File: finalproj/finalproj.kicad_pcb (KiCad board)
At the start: 2 copper layers, 99.2 x 99.6 mm, 83 parts, among them J1 Conn_01x01, J10 MotorA Out, J11 MotorB Out, J2 Conn_01x01, J3 Conn_01x01, J4 Programmer_Conn, J5 Stepper_Motor_Controller, J6 Conn_01x01, J7 LIDAR_Connector, J9 RPI_UART_Conn, SW1 SW_DPDT_x2, SW2 SW_DPDT_x2, SW3 SW_Push, U1 LM1085-12, U2 LM1085-12, U3 LM1085-5.0, U4 LM1085-3.3, U5 L298N, U7 STM32F401RCTx, Y1 25 MHz, Y2 32.768 KHz

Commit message: fixed switch footprints
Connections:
- RV1 pad 1: EXT_GND -> Net-(U3-GND)
- RV1 pad 2: unconnected-(RV1-Pad2) -> EXT_GND
- RV1 pad 3: Net-(U3-GND) -> unconnected-(RV1-Pad3)
- RV3 pad 1: EXT_GND -> Net-(U4-GND)
- RV3 pad 2: unconnected-(RV3-Pad2) -> EXT_GND
- RV3 pad 3: Net-(U4-GND) -> unconnected-(RV3-Pad3)
- RV4 pad 1: EXT_GND -> Net-(U1-GND)
- RV4 pad 2: unconnected-(RV4-Pad2) -> EXT_GND
- RV4 pad 3: Net-(U1-GND) -> unconnected-(RV4-Pad3)
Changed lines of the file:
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@@
   (net 30 "Net-(U7-PH1)")
   (net 31 "Net-(U7-PH0)")
-  (net 32 "unconnected-(RV1-Pad2)")
+  (net 32 "unconnected-(RV1-Pad3)")
   (net 33 "unconnected-(RV2-Pad2)")
-  (net 34 "unconnected-(RV3-Pad2)")
+  (net 34 "unconnected-(RV3-Pad3)")
   (net 35 "unconnected-(U7-PC13-Pad2)")
   (net 36 "unconnected-(U7-PC0-Pad8)")
@@
   (net 80 "Net-(U4-GND)")
   (net 81 "Net-(U1-GND)")
-  (net 82 "unconnected-(RV4-Pad2)")
+  (net 82 "unconnected-(RV4-Pad3)")
   (footprint "Connector_PinHeader_2.54mm:PinHeader_1x01_P2.54mm_Vertical" (layer "F.Cu")
     (at 15.4 46.8 -90)
@@
       (stroke (width 0.1) (type solid)) (fill none) (layer "F.Fab"))
     (pad "1" smd rect (at -1.8 -1) (size 1.2 1.2) (layers "F.Cu" "F.Paste" "F.Mask")
-      (net 3 "EXT_GND") (pinfunction "1") (pintype "passive"))
+      (net 79 "Net-(U3-GND)") (pinfunction "1") (pintype "passive"))
     (pad "2" smd rect (at 1.45 0) (size 1.5 1.6) (layers "F.Cu" "F.Paste" "F.Mask")
-      (net 32 "unconnected-(RV1-Pad2)") (pinfunction "2") (pintype "passive"))
+      (net 3 "EXT_GND") (pinfunction "2") (pintype "passive"))
     (pad "3" smd rect (at -1.8 1) (size 1.2 1.2) (layers "F.Cu" "F.Paste" "F.Mask")
-      (net 79 "Net-(U3-GND)") (pinfunction "3") (pintype "passive"))
+      (net 32 "unconnected-(RV1-Pad3)") (pinfunction "3") (pintype "passive"))
     (model "${KICAD6_3DMODEL_DIR}/Potentiometer_SMD.3dshapes/Potentiometer_Bourns_TC33X_Vertical.wrl"
       (offset (xyz 0 0 0))
@@
       (stroke (width 0.1) (type solid)) (fill none) (layer "F.Fab"))
     (pad "1" smd rect (at -1.8 -1) (size 1.2 1.2) (layers "F.Cu" "F.Paste" "F.Mask")
-      (net 3 "EXT_GND") (pinfunction "1") (pintype "passive"))
+      (net 80 "Net-(U4-GND)") (pinfunction "1") (pintype "passive"))
     (pad "2" smd rect (at 1.45 0) (size 1.5 1.6) (layers "F.Cu" "F.Paste" "F.Mask")
-      (net 34 "unconnected-(RV3-Pad2)") (pinfunction "2") (pintype "passive"))
+      (net 3 "EXT_GND") (pinfunction "2") (pintype "passive"))
     (pad "3" smd rect (at -1.8 1) (size 1.2 1.2) (layers "F.Cu" "F.Paste" "F.Mask")
-      (net 80 "Net-(U4-GND)") (pinfunction "3") (pintype "passive"))
+      (net 34 "unconnected-(RV3-Pad3)") (pinfunction "3") (pintype "passive"))
     (model "${KICAD6_3DMODEL_DIR}/Potentiometer_SMD.3dshapes/Potentiometer_Bourns_TC33X_Vertical.wrl"
       (offset (xyz 0 0 0))
@@
       (stroke (width 0.1) (type solid)) (fill none) (layer "F.Fab"))
     (pad "1" smd rect (at -1.8 -1 90) (size 1.2 1.2) (layers "F.Cu" "F.Paste" "F.Mask")
-      (net 3 "EXT_GND") (pinfunction "1") (pintype "passive"))
+      (net 81 "Net-(U1-GND)") (pinfunction "1") (pintype "passive"))
     (pad "2" smd rect (at 1.45 0 90) (size 1.5 1.6) (layers "F.Cu" "F.Paste" "F.Mask")
-      (net 82 "unconnected-(RV4-Pad2)") (pinfunction "2") (pintype "passive"))
+      (net 3 "EXT_GND") (pinfunction "2") (pintype "passive"))
     (pad "3" smd rect (at -1.8 1 90) (size 1.2 1.2) (layers "F.Cu" "F.Paste" "F.Mask")
-      (net 81 "Net-(U1-GND)") (pinfunction "3") (pintype "passive"))
+      (net 82 "unconnected-(RV4-Pad3)") (pinfunction "3") (pintype "passive"))
     (model "${KICAD6_3DMODEL_DIR}/Potentiometer_SMD.3dshapes/Potentiometer_Bourns_TC33X_Vertical.wrl"
       (offset (xyz 0 0 0))

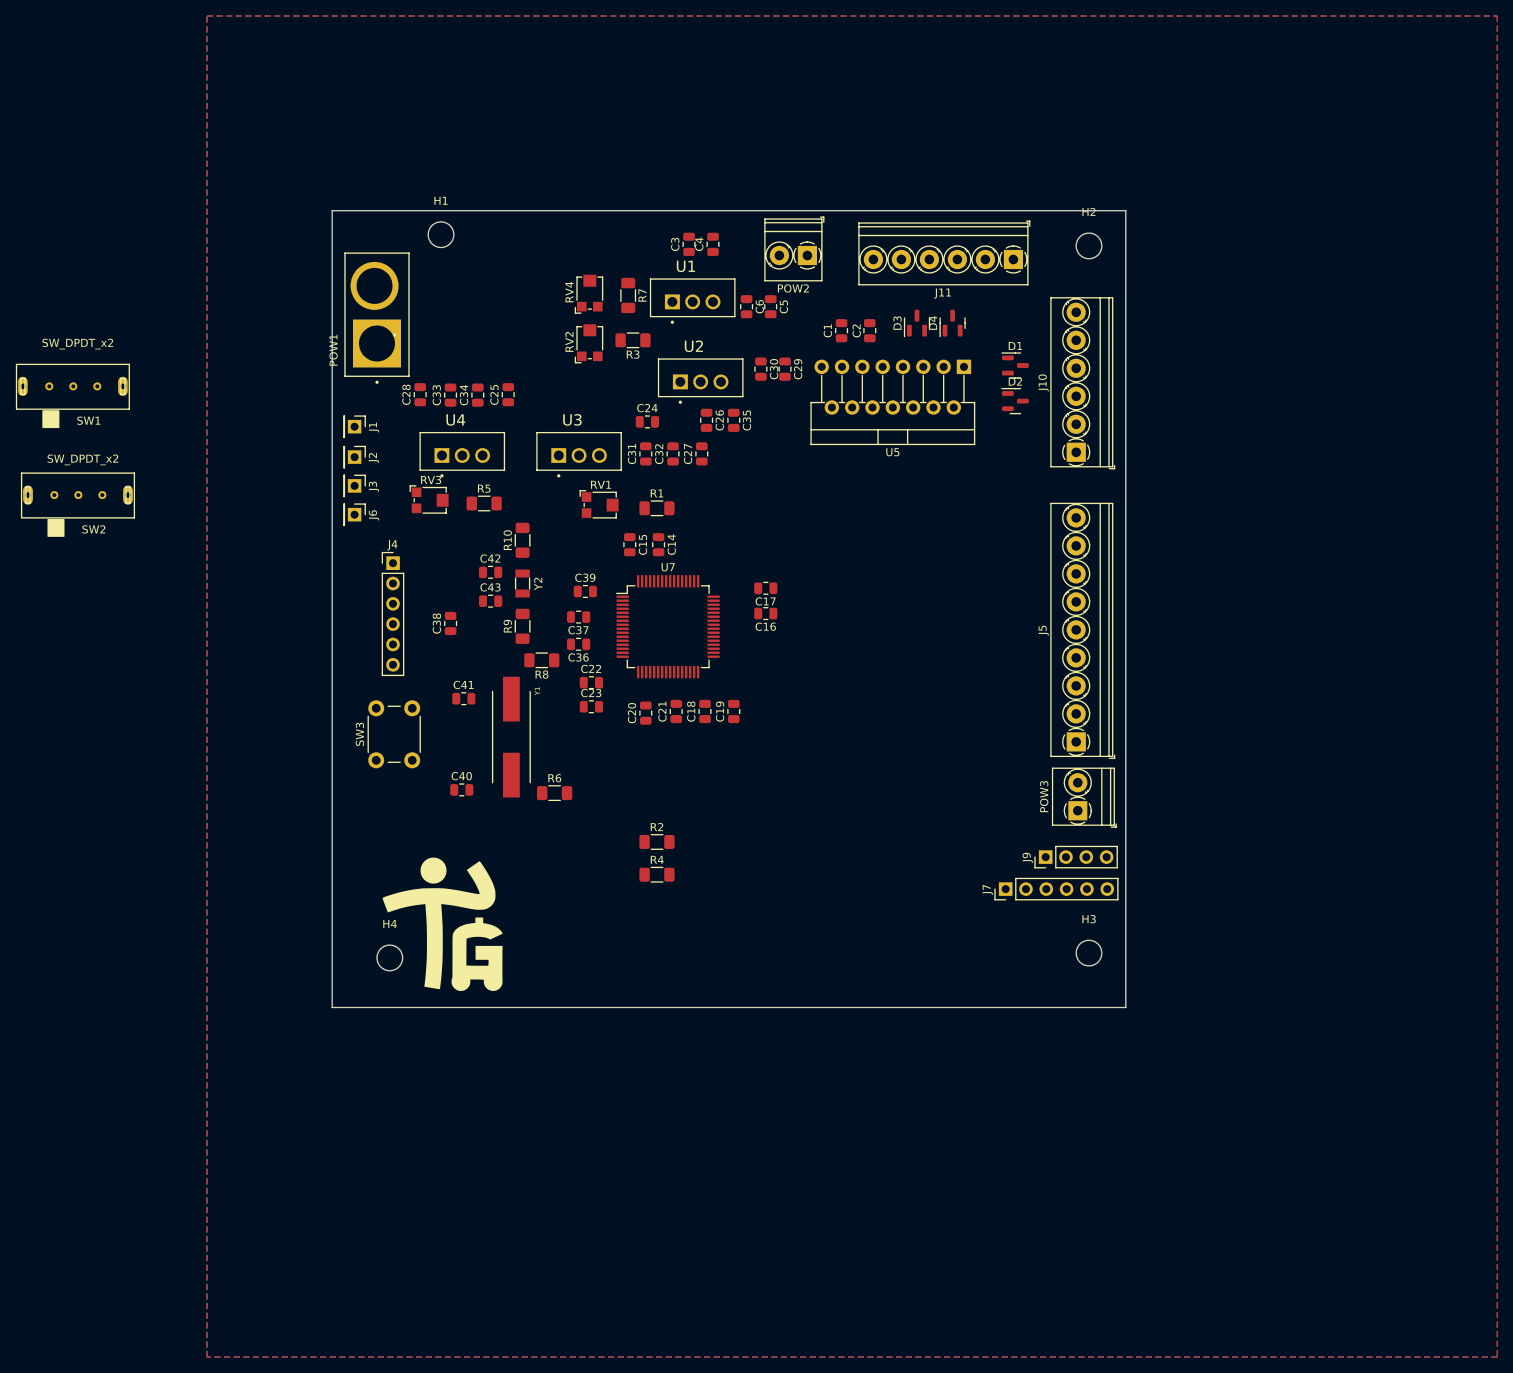
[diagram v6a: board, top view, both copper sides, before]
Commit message: made initial placement for each component on PCB, connected MCU passive components
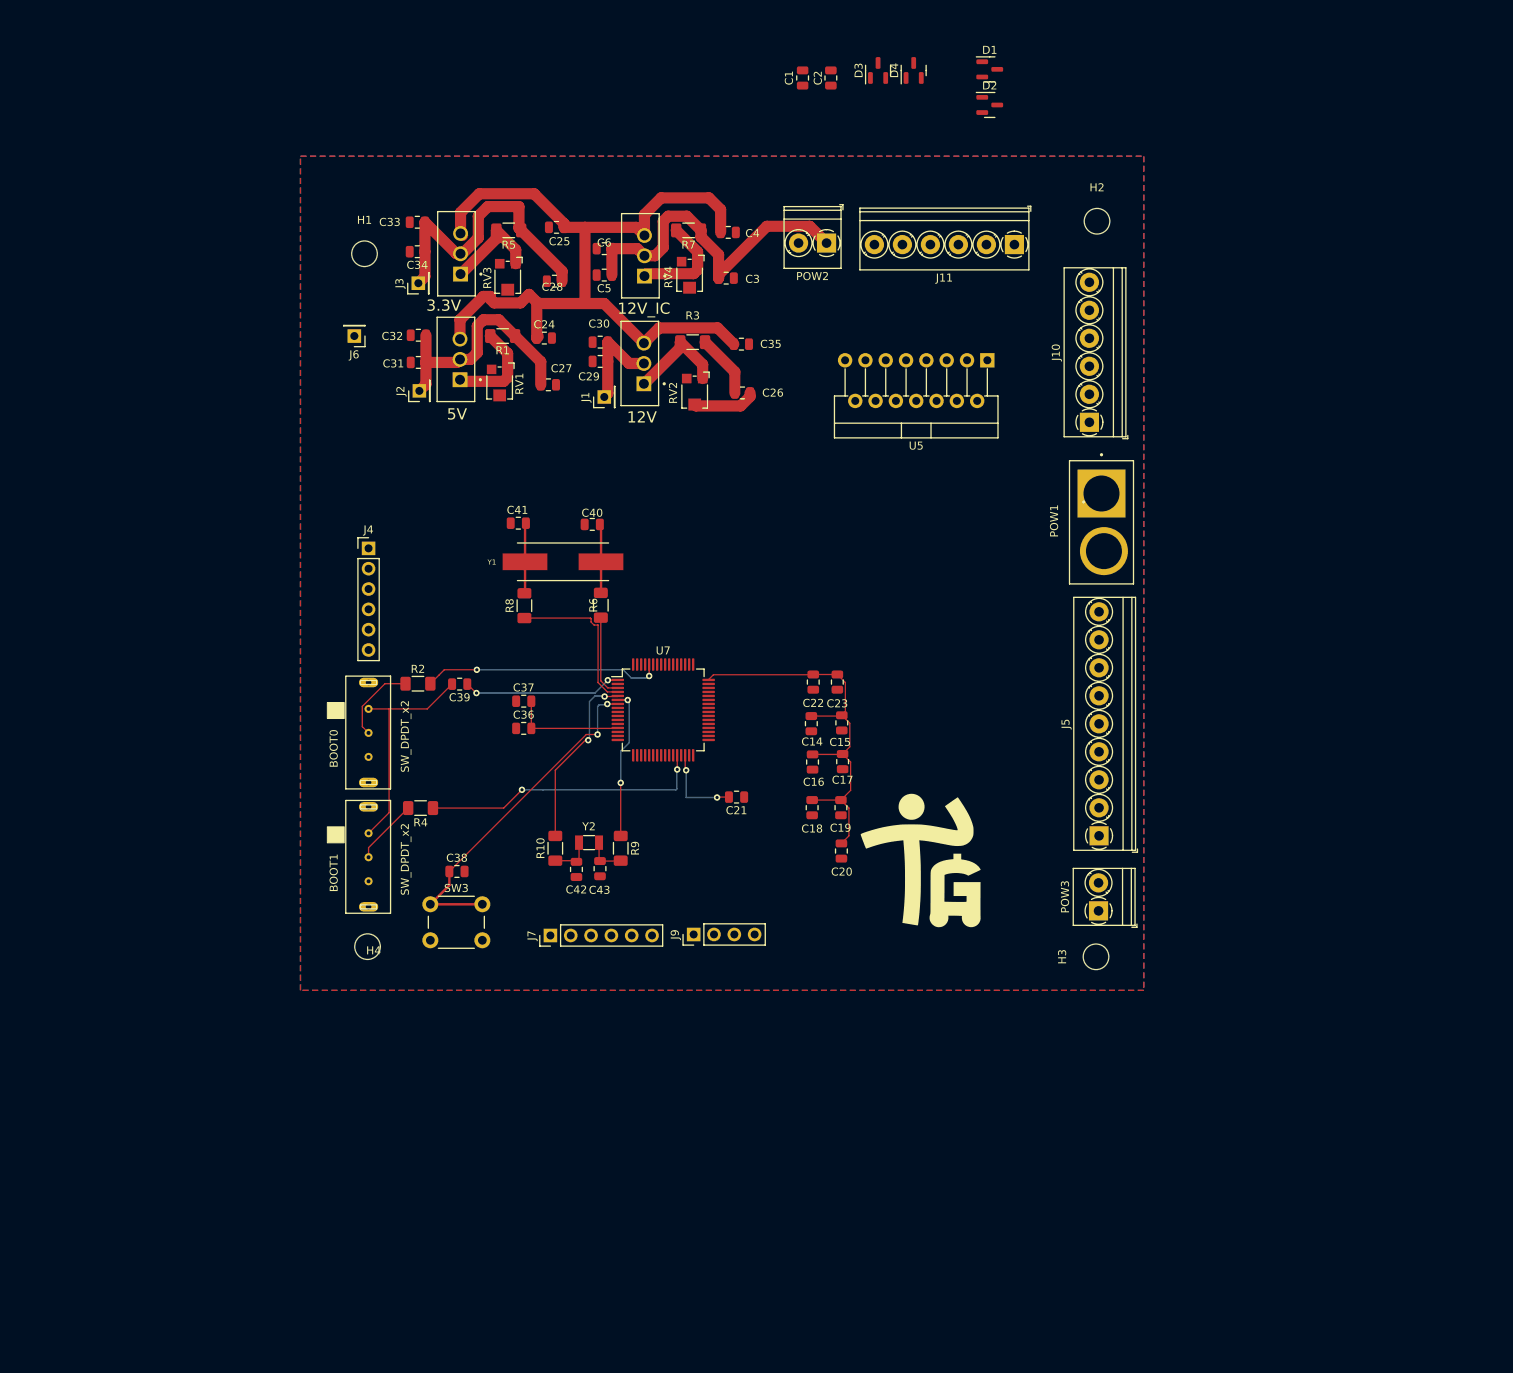
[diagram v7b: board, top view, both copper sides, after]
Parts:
- removed SW1, SW2: SW_DPDT_x2, Switch_E-Switch_EG1206A:SLIDE-SWITCH
- added BOOT0: SW_DPDT_x2, Switch_E-Switch_EG1206A:SLIDE-SWITCH, F.Cu at (16.0, 71.4)
- added BOOT1: SW_DPDT_x2, Switch_E-Switch_EG1206A:SLIDE-SWITCH, F.Cu at (16.0, 86.9)
- moved POW1 94.2 mm to (108.8, 51.4), turned to -90 degrees
- moved G*** 60.3 mm to (87.7, 94.1)
- moved J7 57.2 mm to (39.9, 103.0)
- moved J9 45.0 mm to (57.8, 102.9)
- moved R10 38.7 mm to (40.5, 92.1)
- moved C42 38.7 mm to (43.1, 94.7), turned to 90 degrees
- moved D1 37.2 mm to (94.8, -5.27)
- moved D2 37.2 mm to (94.8, -0.82)
- moved C40 37.0 mm to (45.1, 51.6)
- moved C43 36.1 mm to (46.1, 94.6), turned to 90 degrees
- moved R2 35.8 mm to (23.3, 71.5)
- moved C32 35.1 mm to (23.4, 28.0), turned to 180 degrees
- moved C15 34.6 mm to (76.3, 76.4), turned to 90 degrees
- moved R5 34.3 mm to (34.7, 14.9), turned to 180 degrees
- moved Y2 33.4 mm to (44.7, 91.4), turned to 0 degrees
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- renumbered U2 to 12V, U1 to 12V_IC, U4 to 3.3V, U3 to 5V
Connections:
- RV2 pad 1: EXT_GND -> Net-(U2-GND)
- RV2 pad 2: unconnected-(RV2-Pad2) -> EXT_GND
- RV2 pad 3: Net-(U2-GND) -> unconnected-(RV2-Pad3)
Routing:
- net EXT_3.3: track 0.00 -> 117.1 mm
- net BATTERY_VIN: track 0.00 -> 103.1 mm
- net 12V_IC: track 0.00 -> 43.7 mm
- net NRST: track 0.00 -> 43.4 mm, vias 0 -> 2
- net Net-(U7-PB2): track 0.00 -> 35.7 mm, vias 0 -> 2
- net EXT_5: track 0.00 -> 30.9 mm
- net Net-(U7-BOOT0): track 0.00 -> 30.0 mm, vias 0 -> 2
- net Net-(U7-PH0): track 0.00 -> 22.7 mm, vias 0 -> 2
- net EXT_12: track 0.00 -> 20.5 mm
- net Net-(U7-VBAT): track 0.00 -> 20.1 mm, vias 0 -> 2
- net Net-(U7-PC15): track 0.00 -> 19.9 mm
- net Net-(U7-PH1): track 0.00 -> 18.7 mm, vias 0 -> 2
- net Net-(U7-VREF+): track 0.00 -> 14.2 mm
- net Net-(U1-GND): track 0.00 -> 13.0 mm
- net Net-(U2-GND): track 0.00 -> 12.8 mm
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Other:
- board outline removed

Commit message: made most MCU connectioins
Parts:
- moved D1 68.8 mm to (90.6, 63.4), turned to -90 degrees
- moved D4 66.8 mm to (84.4, 61.6)
- moved D3 62.1 mm to (84.4, 56.9)
- moved D2 59.0 mm to (90.8, 58.0), turned to -90 degrees
- moved C1 45.5 mm to (101.2, 30.2), turned to -90 degrees
- moved C2 30.5 mm to (89.2, 22.8), turned to 0 degrees
- moved U5 8.98 mm to (94.0, 40.1)
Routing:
- net EXT_3.3: track 117.1 -> 228.2 mm, vias 0 -> 8
- net EXT_5: track 30.9 -> 115.1 mm
- net SWDIO: track 0.00 -> 56.7 mm, vias 0 -> 2
- net SWCLK: track 0.00 -> 51.5 mm, vias 0 -> 2
- net NRST: track 43.4 -> 94.4 mm
- net RPI_UART_RX: track 0.00 -> 48.0 mm, vias 0 -> 2
- net RPI_UART_TX: track 0.00 -> 42.4 mm, vias 0 -> 2
- net LIDAR_SDA: track 0.00 -> 41.4 mm, vias 0 -> 2
- net SWO: track 0.00 -> 39.5 mm, vias 0 -> 2
- net LIDAR_SCL: track 0.00 -> 39.0 mm, vias 0 -> 2
- net MotorOutA1: track 0.00 -> 21.2 mm
- net MotorOutB2: track 0.00 -> 19.4 mm, vias 0 -> 2
- net MotorOutA2: track 0.00 -> 19.2 mm
- net MotorOutB1: track 0.00 -> 19.0 mm, vias 0 -> 2
- net EXT_12: track 20.5 -> 35.1 mm
